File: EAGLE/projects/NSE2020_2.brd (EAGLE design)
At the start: 80 x 80 mm, 9 parts

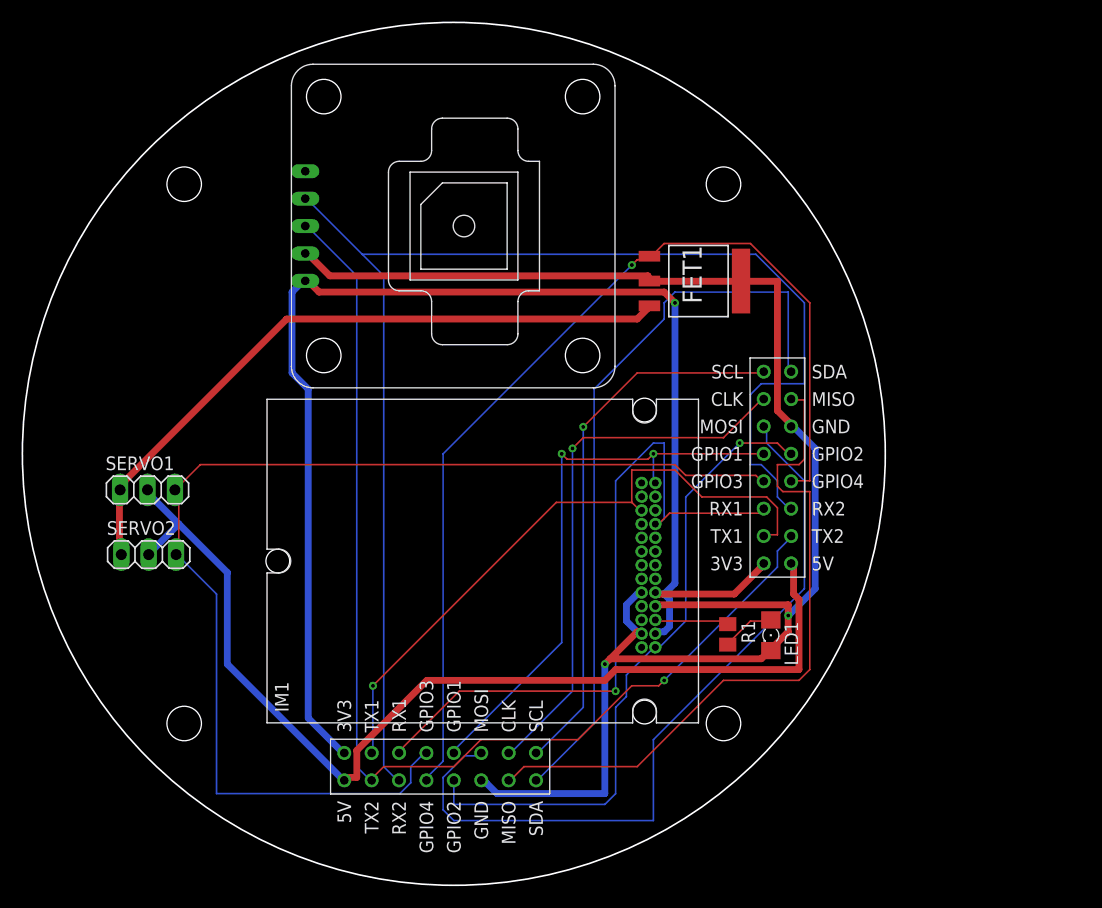
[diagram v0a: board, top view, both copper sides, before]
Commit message: ディレクトリ構成の変更
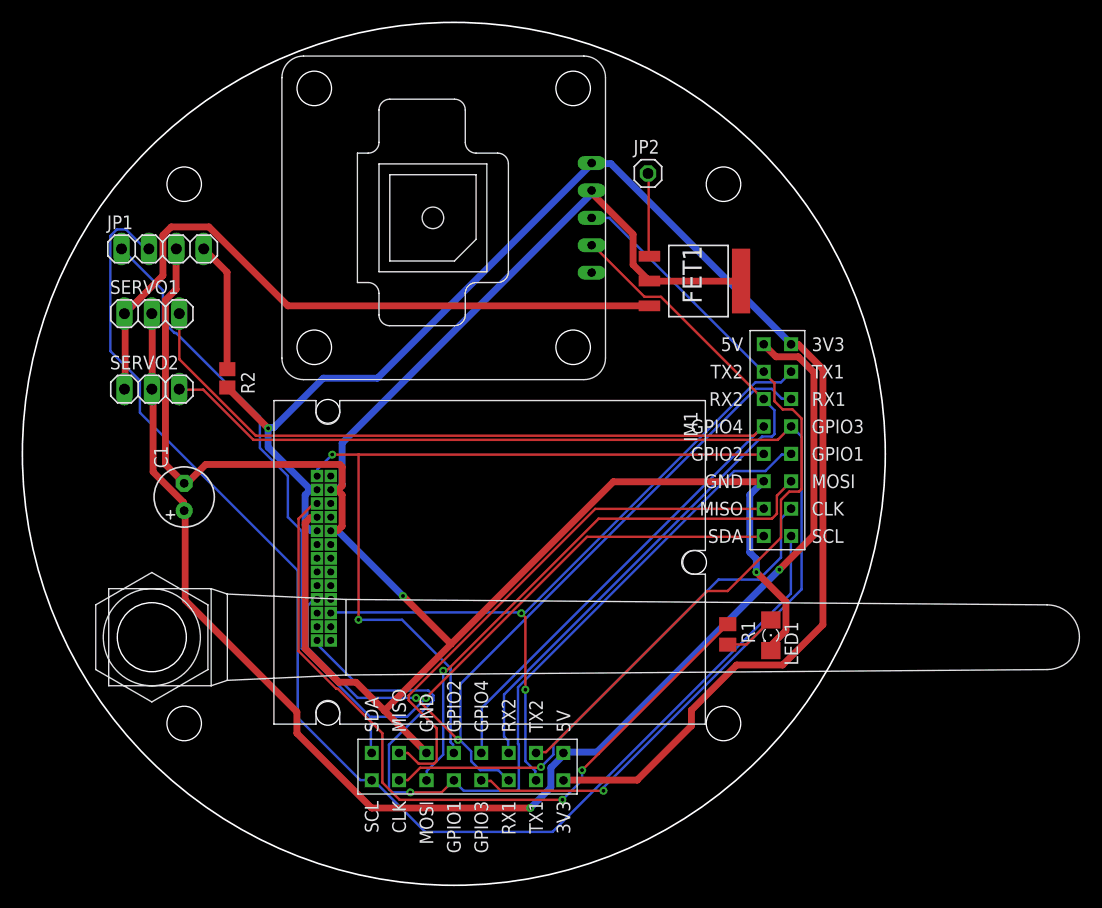
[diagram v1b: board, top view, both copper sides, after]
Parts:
- added ANT1: IM920ANT-XS, IM920ANT-XS:ANTENNA
- added C1: 100u, rcl:E2,5-6
- added JP1: (no value), pinhead:1X04
- added JP2: (no value), pinhead:1X01
- added R2: 330, rcl:R2012
- moved SERVO1 16.3 mm to (12.0, 53.0)
- moved SERVO2 15.3 mm to (12.0, 46.0)
- moved GPS 1.16 mm to (39.1, 61.9), turned to 0 degrees
- moved IM1 0.65 mm to (43.3, 29.9), turned to 270 degrees
- turned BUS1 to 90 degrees
- turned BUS2 to 180 degrees
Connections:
- net N$3 renamed CLK
- net N$4 renamed MISO
- net N$5 renamed MOSI
- removed net N$1: BUS1.P0, BUS2.P0
- removed net N$2: BUS1.P13, BUS2.P13
- removed net PWM: BUS1.P14, BUS2.P14, SERVO1.3, SERVO2.3
- removed net SERVOGATE: BUS1.P15, BUS2.P15, FET1.P$3
- new net PWM1: BUS1.P14, BUS2.P14, SERVO2.3
- new net PWM2: BUS1.P15, BUS2.P15, SERVO1.3
- new net R2BMP: JP1.4, R2.1
- new net SCL: BUS1.P0, BUS2.P0, JP1.2
- new net SDA: BUS1.P13, BUS2.P13, JP1.1
- new net SERVO_GATE: FET1.P$3, JP2.1
- net +3V3: now also R2.2
- net BAT: now also C1.+
- net GND: now also C1.-, JP1.3
- net RX1: now also BUS1.P4, BUS2.P4, IM1.IO10; no longer BUS1.P5, BUS2.P5, IM1.IO16
- net RX2: now also BUS1.P9, BUS2.P9, GPS.P4; no longer BUS1.P8, BUS2.P8, GPS.P3
- net TX1: now also BUS1.P5, BUS2.P5, IM1.IO16; no longer BUS1.P4, BUS2.P4, IM1.IO10
- net TX2: now also BUS1.P8, BUS2.P8, GPS.P3; no longer BUS1.P9, BUS2.P9, GPS.P4
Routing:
- net SCL: track 0.00 -> 121.0 mm
- net PWM1: track 0.00 -> 112.7 mm, vias 0 -> 1
- net PWM: track 108.1 -> 0.00 mm
- net PWM2: track 0.00 -> 102.8 mm
- net SDA: track 0.00 -> 99.8 mm, vias 0 -> 1
- net SERVOGATE: track 93.5 -> 0.00 mm, vias 1 -> 0
- net N$2: track 68.6 -> 0.00 mm
- net GND: track 144.8 -> 209.2 mm
- net IM2R: track 6.82 -> 70.1 mm, vias 0 -> 2
- net TX2: track 126.2 -> 71.6 mm
- net N$1: track 50.9 -> 0.00 mm, vias 1 -> 0
- net RX2: track 103.3 -> 66.2 mm, vias 1 -> 0
- net BAT: track 96.6 -> 127.8 mm, vias 0 -> 2
- net BUSY: track 53.8 -> 80.4 mm, vias 2 -> 1
- net MOSI: track 71.5 -> 51.3 mm, vias 0 -> 1
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
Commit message: IM920修正
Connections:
- net +3V3: now also IM1.IO17, IM1.IO23; no longer IM1.IO2, IM1.IO5
- net BUSY: now also IM1.IO1; no longer IM1.IO13
- net GND: now also IM1.IO18, IM1.IO19, IM1.IO24; no longer IM1.IO22, IM1.IO25, IM1.IO4
- net IM2R: now also IM1.IO21; no longer IM1.IO3
- net RESET: now also IM1.IO25; no longer IM1.IO1
- net RX1: now also IM1.IO7; no longer IM1.IO10
- net TX1: now also IM1.IO6; no longer IM1.IO16
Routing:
- net TX1: track 68.1 -> 95.4 mm, vias 2 -> 1
- net RX2: track 66.2 -> 83.7 mm, vias 0 -> 1
- net GND: track 209.2 -> 192.8 mm, vias 2 -> 0
- net PWM1: track 112.7 -> 128.2 mm, vias 1 -> 0
- net RX1: track 77.0 -> 91.3 mm
- net SDA: track 99.8 -> 113.2 mm
- net PWM2: track 102.8 -> 90.0 mm, vias 0 -> 2
- net MOSI: track 51.3 -> 62.6 mm, vias 1 -> 0
- net IM2R: track 70.1 -> 59.0 mm, vias 2 -> 1
- net BUSY: track 80.4 -> 72.0 mm, vias 1 -> 2
- net CLK: track 49.4 -> 57.5 mm, vias 1 -> 0
- net GND2FET: track 64.3 -> 57.5 mm, vias 0 -> 1
- net MISO: track 51.2 -> 57.9 mm
- net R2LED: track 4.95 -> 11.5 mm
- net SCL: track 121.0 -> 126.1 mm, vias 0 -> 1
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
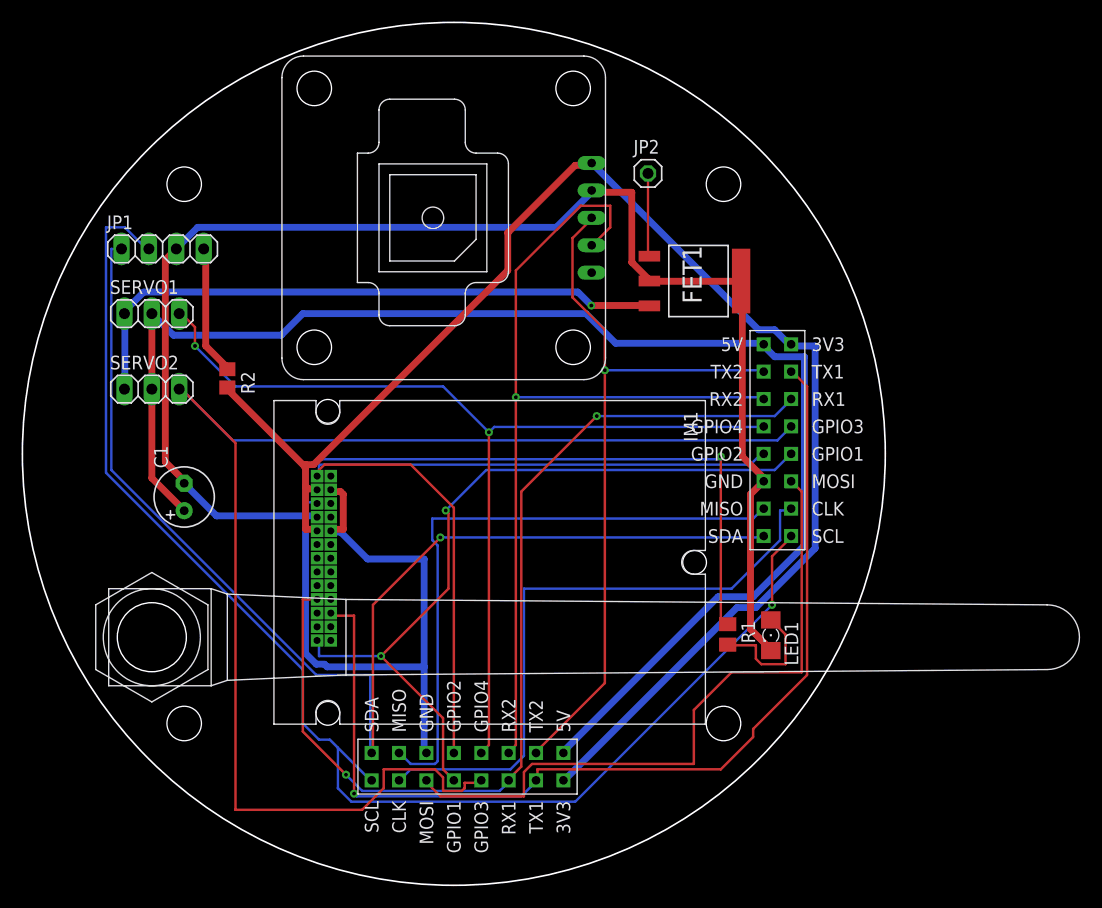
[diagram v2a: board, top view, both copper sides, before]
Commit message: 第2次試作で見つかったミスの修正
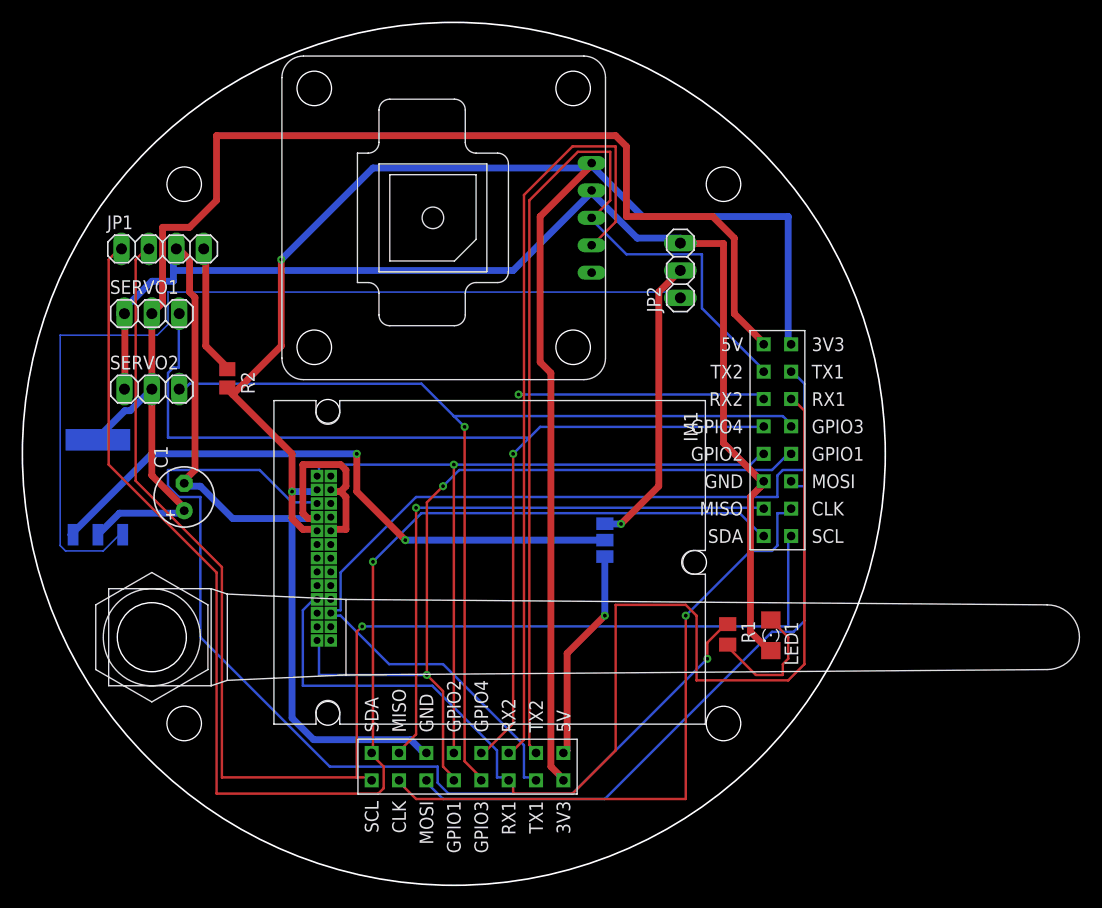
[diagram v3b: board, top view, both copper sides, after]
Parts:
- removed FET1: 2SK4033, 2SK4033:2SK4033
- added SJ1: (no value), jumper:SJ_2
- added U$1: 2SJ681, 2SJ681:2SJ681
- JP2: device pinhead:1X01 -> pinhead:1X03
- moved JP2 9.49 mm to (61.0, 57.0), turned to 90 degrees
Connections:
- removed net GND2FET: FET1.P$4, SERVO1.1, SERVO2.1
- removed net SERVO_GATE: FET1.P$3, JP2.1
- new net 5V_CELL: BUS1.P7, SJ1.1
- new net BAT_CELL: JP2.2, SJ1.3
- new net N$1: SJ1.2, U$1.P$3
- new net N$2: JP2.1, U$1.P$1
- net BAT: now also U$1.P$2, U$1.P$4; no longer BUS1.P7
- net GND: now also JP2.3, SERVO1.1, SERVO2.1; no longer FET1.P$1, FET1.P$2
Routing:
- net N$2: track 0.00 -> 87.3 mm
- net N$1: track 0.00 -> 58.2 mm, vias 0 -> 2
- net GND2FET: track 57.5 -> 0.00 mm, vias 1 -> 0
- net IM2R: track 59.0 -> 96.1 mm
- net PWM1: track 128.2 -> 93.5 mm, vias 0 -> 1
- net BAT_CELL: track 0.00 -> 27.3 mm, vias 0 -> 1
- net TX2: track 69.0 -> 92.6 mm, vias 1 -> 0
- net +3V3: track 137.7 -> 159.0 mm, vias 0 -> 2
- net 5V_CELL: track 0.00 -> 19.8 mm, vias 0 -> 1
- net SDA: track 113.2 -> 131.4 mm
- net RX1: track 91.3 -> 108.8 mm, vias 2 -> 0
- net RX2: track 83.7 -> 96.3 mm
- net RESET: track 80.6 -> 69.6 mm, vias 0 -> 1
- net GND: track 192.8 -> 201.9 mm
- net PWM2: track 90.0 -> 99.1 mm, vias 2 -> 1
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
